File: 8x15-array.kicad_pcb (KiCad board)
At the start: 2 copper layers, 75 x 50 mm, 240 parts, among them P1 CONN_01X01, P10 CONN_01X01, P100 CONN_01X01, P101 CONN_01X01, P102 CONN_01X01, P103 CONN_01X01, P104 CONN_01X01, P105 CONN_01X01, P106 CONN_01X01, P107 CONN_01X01, P108 CONN_01X01, P109 CONN_01X01, P11 CONN_01X01, P110 CONN_01X01, P111 CONN_01X01, P112 CONN_01X01, P113 CONN_01X01, P114 CONN_01X01, P115 CONN_01X01, P116 CONN_01X01, P117 CONN_01X01, P118 CONN_01X01, P119 CONN_01X01, P12 CONN_01X01, P120 CONN_01X01, P13 CONN_01X01, P14 CONN_01X01, P15 CONN_01X01, P16 CONN_01X01, P17 CONN_01X01, P18 CONN_01X01, P19 CONN_01X01, P2 CONN_01X01, P20 CONN_01X01, P21 CONN_01X01, P22 CONN_01X01, P23 CONN_01X01, P24 CONN_01X01, P25 CONN_01X01, P26 CONN_01X01, P27 CONN_01X01, P28 CONN_01X01, P29 CONN_01X01, P3 CONN_01X01, P30 CONN_01X01, P31 CONN_01X01, P32 CONN_01X01, P33 CONN_01X01, P34 CONN_01X01, P35 CONN_01X01, P36 CONN_01X01, P37 CONN_01X01, P38 CONN_01X01, P39 CONN_01X01, P4 CONN_01X01, P40 CONN_01X01, P41 CONN_01X01, P42 CONN_01X01, P43 CONN_01X01, P44 CONN_01X01, P45 CONN_01X01, P46 CONN_01X01, P47 CONN_01X01, P48 CONN_01X01, P49 CONN_01X01, P5 CONN_01X01, P50 CONN_01X01, P51 CONN_01X01, P52 CONN_01X01, P53 CONN_01X01, P54 CONN_01X01, P55 CONN_01X01, P56 CONN_01X01, P57 CONN_01X01, P58 CONN_01X01, P59 CONN_01X01, P6 CONN_01X01, P60 CONN_01X01, P61 CONN_01X01, P62 CONN_01X01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

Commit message: Finish making connections
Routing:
- net Net-(E116-Pad1): track 0.72 -> 35.9 mm
- net Net-(E112-Pad1): track 0.72 -> 35.8 mm
- net Net-(E59-Pad1): track 0.77 -> 35.8 mm
- net Net-(E108-Pad1): track 0.72 -> 35.7 mm
- net Net-(E104-Pad1): track 0.72 -> 35.6 mm
- net Net-(E51-Pad1): track 0.77 -> 35.6 mm
- net Net-(E100-Pad1): track 0.72 -> 35.5 mm
- net Net-(E60-Pad1): track 0.72 -> 35.4 mm
- net Net-(E55-Pad1): track 0.77 -> 35.5 mm
- net Net-(E64-Pad1): track 0.72 -> 35.4 mm
- net Net-(E96-Pad1): track 0.72 -> 35.4 mm
- net Net-(E35-Pad1): track 0.77 -> 35.3 mm
- net Net-(E92-Pad1): track 0.72 -> 35.3 mm
- net Net-(E47-Pad1): track 0.77 -> 35.3 mm
- net Net-(E68-Pad1): track 0.72 -> 35.2 mm
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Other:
- net class Default: clearance 0.1 -> 0.15; trace_width 0.15 -> 0.1; via_dia 0.762 -> 0.3; via_drill 0.381 -> 0.15
- rule trace_clearance: 0.1 -> 0.15
- rule trace_min: 0.15 -> 0.1
- rule via_min_drill: 0.381 -> 0.15
- rule via_min_size: 0.762 -> 0.3
- board text added: "8x15-array, v0.1"
- board text removed: "120-channel-array, v0.1"

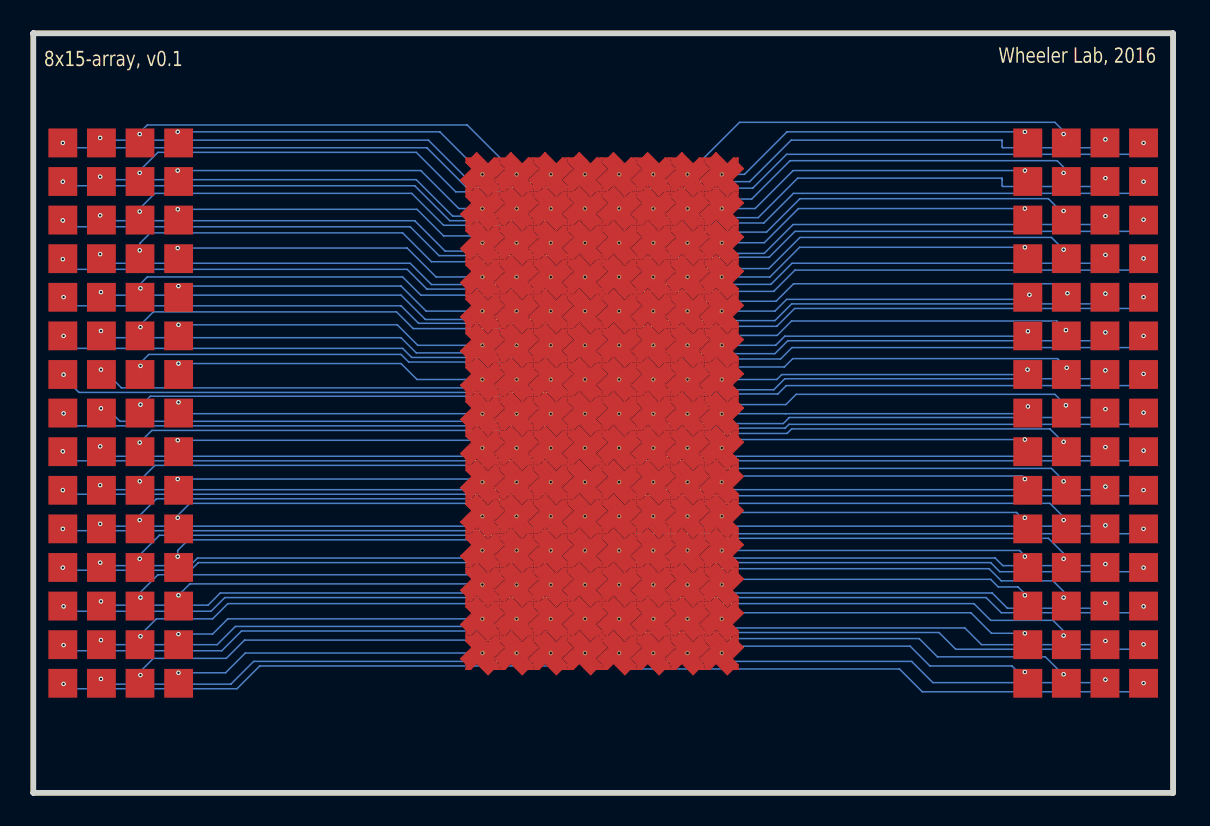
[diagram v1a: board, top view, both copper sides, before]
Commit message: Update to use through-hole contact pads
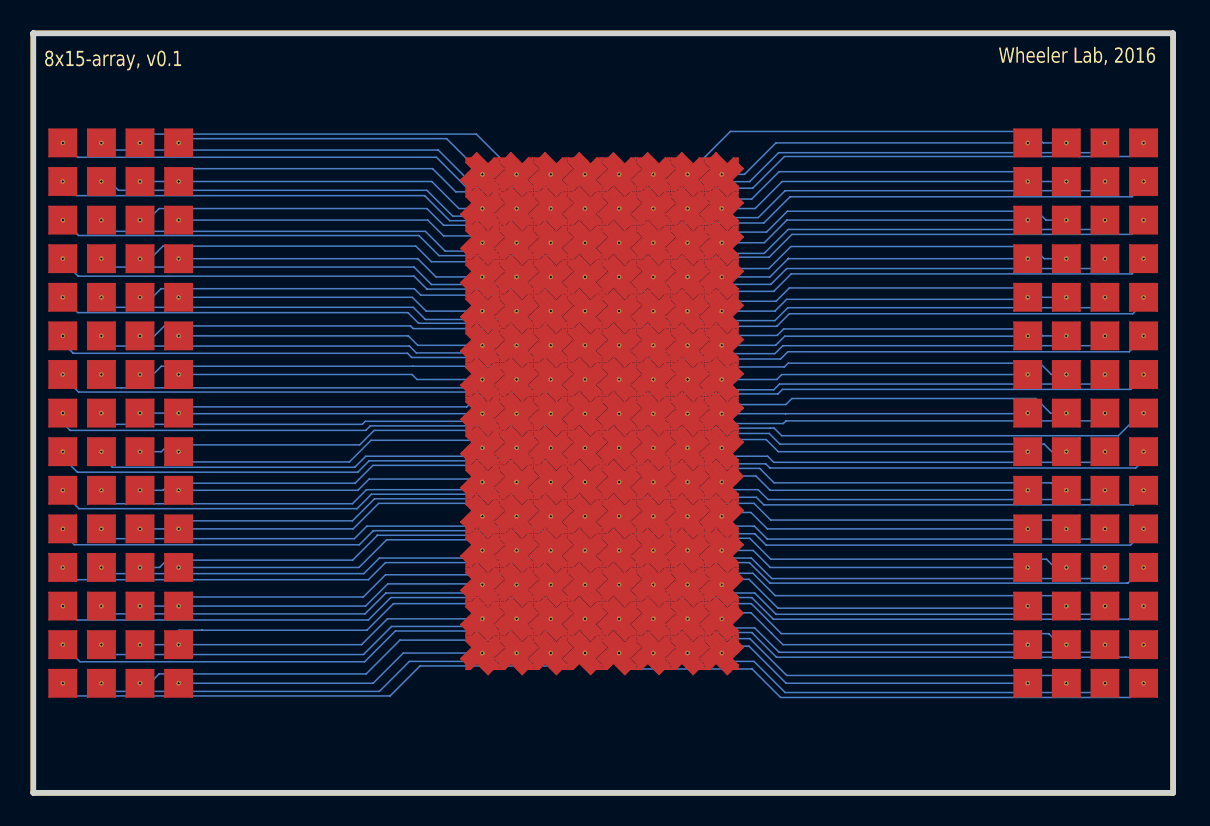
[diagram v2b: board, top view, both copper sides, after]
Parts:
- P1, P10, P100, P101, P102, P103, P104, P105, P106, P107, P108, P109, P11, P110, P111, P112, P113, P114, P115, P116, P117, P118, P119, P12, P120, P13, P14, P15, P16, P17, P18, P19, P2, P20, P21, P22, P23, P24, P25, P26, P27, P28, P29, P3, P30, P31, P32, P33, P34, P35, P36, P37, P38, P39, P4, P40, P41, P42, P43, P44, P45, P46, P47, P48, P49, P5, P50, P51, P52, P53, P54, P55, P56, P57, P58, P59, P6, P60, P61, P62, P63, P64, P65, P66, P67, P68, P69, P7, P70, P71, P72, P73, P74, P75, P76, P77, P78, P79, P8, P80, P81, P82, P83, P84, P85, P86, P87, P88, P89, P9, P90, P91, P92, P93, P94, P95, P96, P97, P98, P99: footprint WheelerLab:1.9mm_DMF_Electrode -> WheelerLab:1.9mm_DMF_Electrode-hole
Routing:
- net Net-(E106-Pad1): track 27.3 -> 26.0 mm, vias 1 -> 0
- net Net-(E114-Pad1): track 27.6 -> 26.2 mm, vias 1 -> 0
- net Net-(E110-Pad1): track 27.3 -> 26.0 mm, vias 1 -> 0
- net Net-(E2-Pad1): track 32.3 -> 31.0 mm, vias 1 -> 0
- net Net-(E6-Pad1): track 32.4 -> 31.1 mm, vias 1 -> 0
- net Net-(E98-Pad1): track 26.8 -> 25.6 mm, vias 1 -> 0
- net Net-(E102-Pad1): track 26.8 -> 25.6 mm, vias 1 -> 0
- net Net-(E94-Pad1): track 26.4 -> 25.4 mm, vias 1 -> 0
- net (no net): track 0.00 -> 1.07 mm
- net Net-(E28-Pad1): track 21.2 -> 20.2 mm, vias 1 -> 0
- net Net-(E76-Pad1): track 34.9 -> 35.8 mm, vias 1 -> 0
- net Net-(E84-Pad1): track 35.0 -> 35.9 mm, vias 1 -> 0
- net Net-(E118-Pad1): track 27.0 -> 26.1 mm, vias 1 -> 0
- net Net-(E80-Pad1): track 34.9 -> 35.8 mm, vias 1 -> 0
- net Net-(E21-Pad1): track 26.5 -> 25.6 mm, vias 1 -> 0
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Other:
- rule pad_to_mask_clearance: 0.254 -> 0
